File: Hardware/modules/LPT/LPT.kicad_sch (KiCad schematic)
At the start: 17 parts, among them J1 DB25_Receptacle, J2 Bus_PCI_6502, U1 74HC138, U2 74HC138, U3 74HC00, U4 74AHC541, U5 74HCT574, U6 74HCT574, U7 74HC02

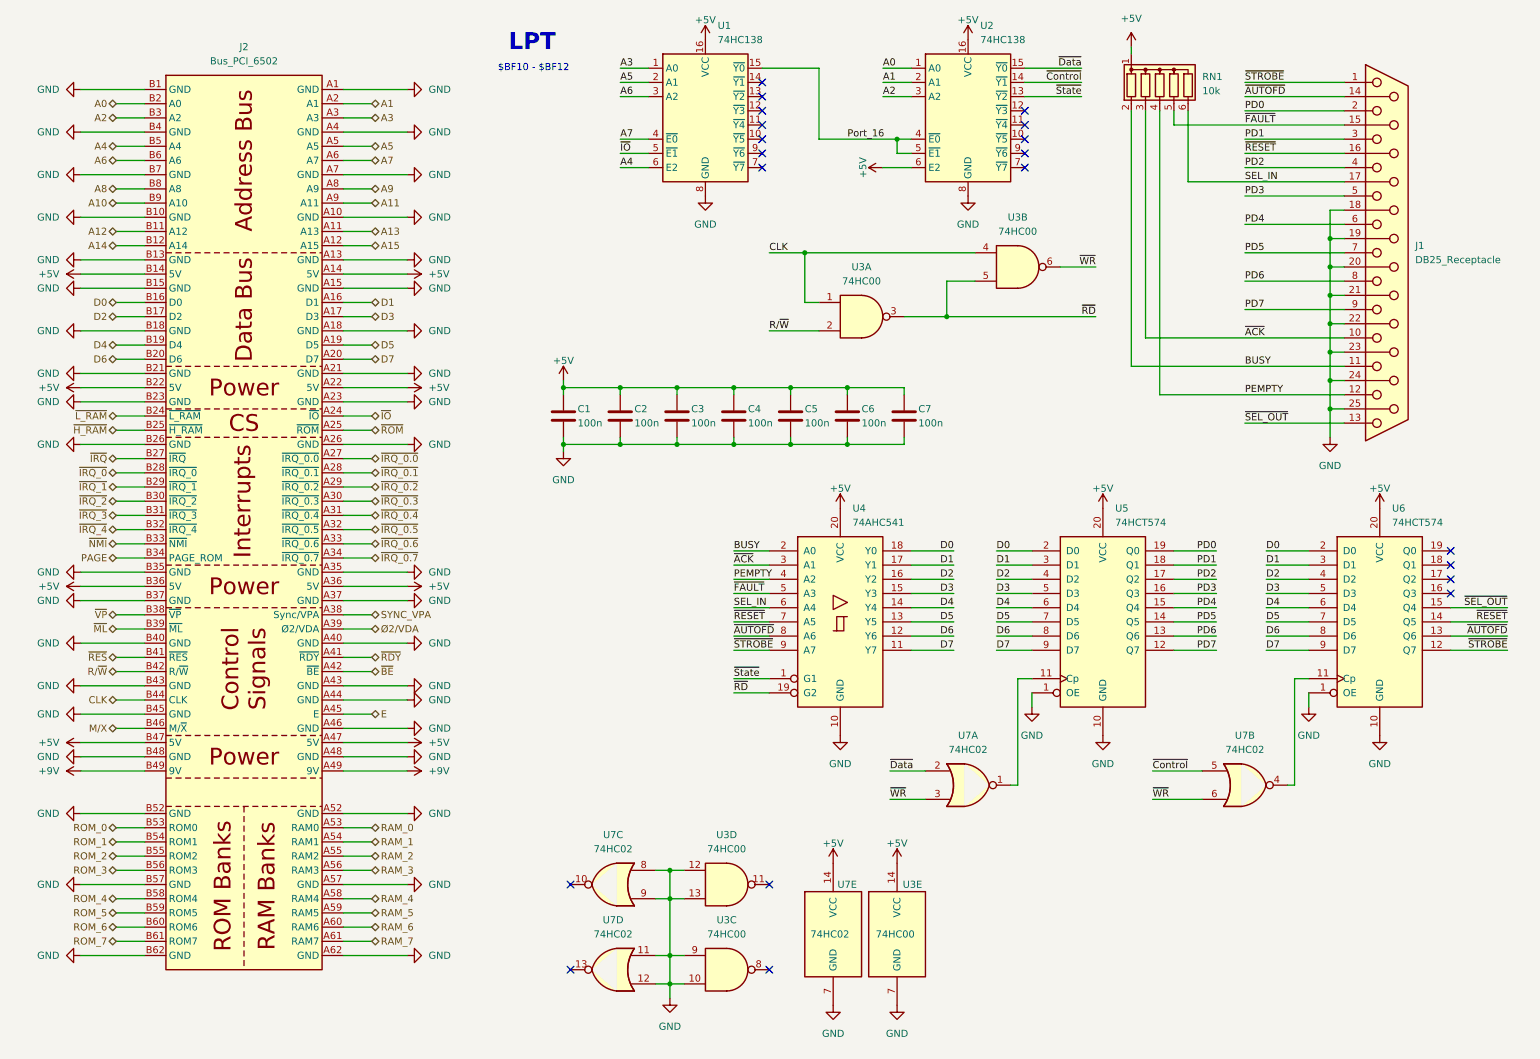
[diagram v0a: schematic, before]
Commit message: Hardware Update Add MyCPU VGA Module Beautify all Schematics minor Error corrections Readme Update
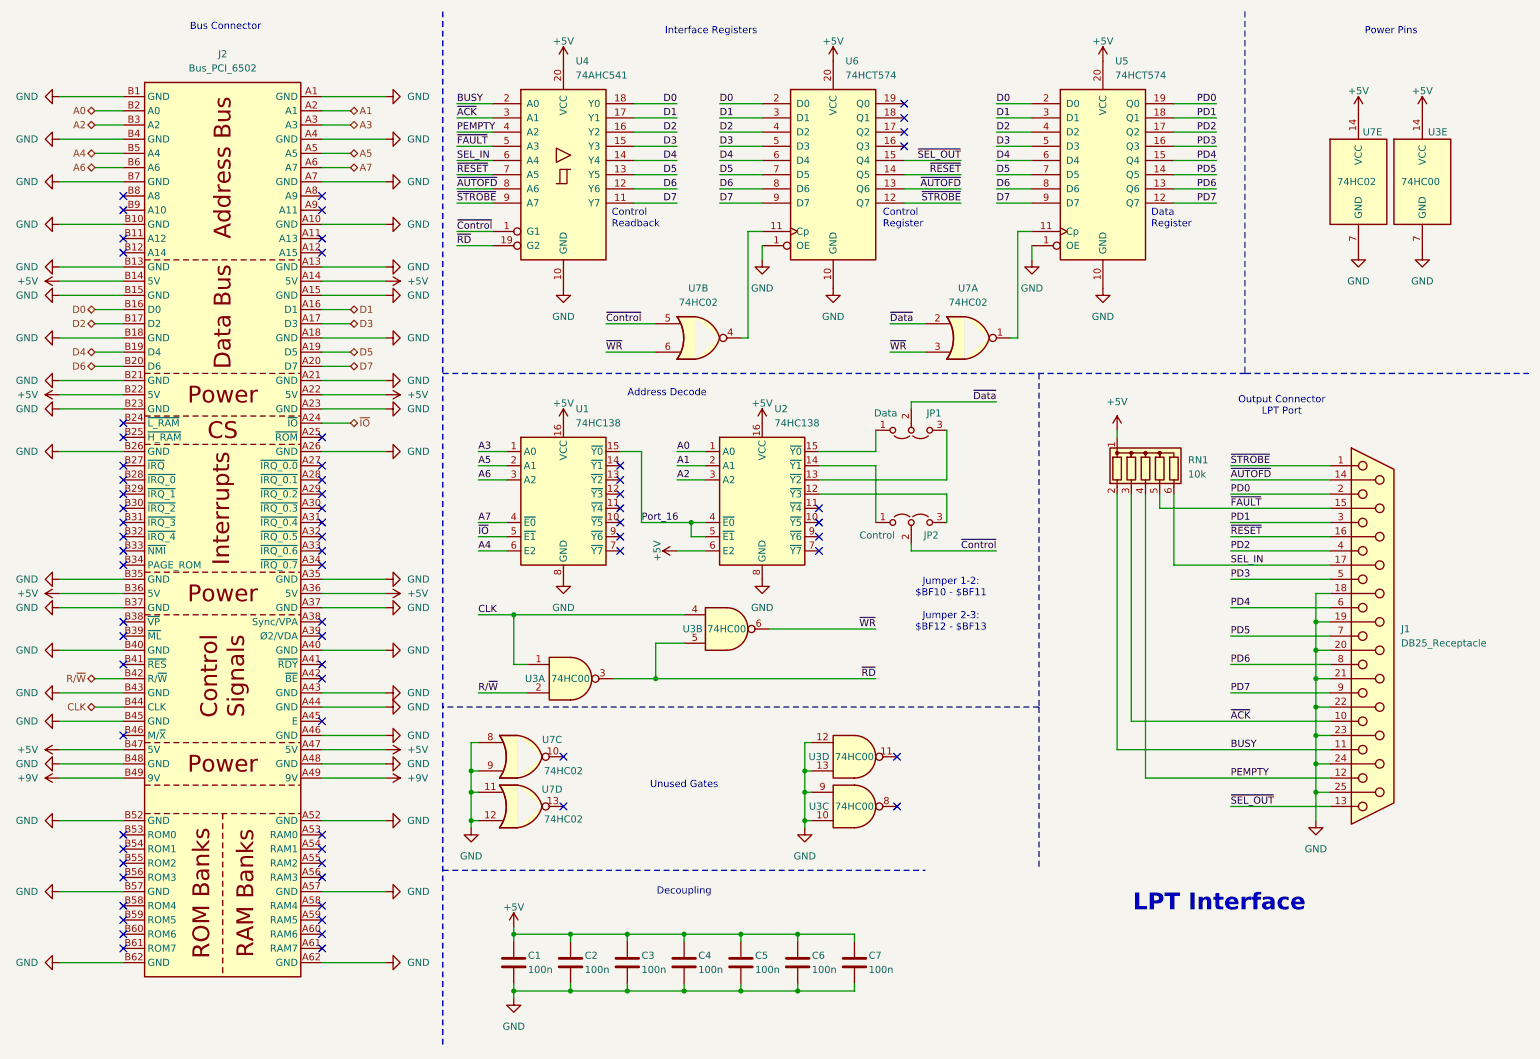
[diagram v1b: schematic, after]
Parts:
- added JP1: Data, Jumper:SolderJumper-3_P2.0mm_Open_TrianglePad1.0x1.5mm_NumberLabels, symbol Jumper:Jumper_3_Open
- added JP2: Control, Jumper:SolderJumper-3_P2.0mm_Open_TrianglePad1.0x1.5mm_NumberLabels, symbol Jumper:Jumper_3_Open
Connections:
- net ~{Control}: now also U4.1 (G1), JP2.2 (C); no longer U2.14 (~{Y1})
- net ~{Data}: now also JP1.2 (C); no longer U2.15 (~{Y0})
- net at U2.12 (~{Y3}): now also JP2.3 (B)
- net A10: no longer names the net of J2.B9 (A10)
- net A11: no longer names the net of J2.A9 (A11)
- net A12: no longer names the net of J2.B11 (A12)
- net A13: no longer names the net of J2.A11 (A13)
- net A14: no longer names the net of J2.B12 (A14)
- net A15: no longer names the net of J2.A12 (A15)
- net A8: no longer names the net of J2.B8 (A8)
- net A9: no longer names the net of J2.A8 (A9)
- net E: no longer names the net of J2.A45 (E)
- net M/X: no longer names the net of J2.B46 (M/~{X})
- net PAGE: no longer names the net of J2.B34 (PAGE_ROM)
- net RAM_0: no longer names the net of J2.A53 (RAM0)
- net RAM_1: no longer names the net of J2.A54 (RAM1)
- net RAM_2: no longer names the net of J2.A55 (RAM2)
- net RAM_3: no longer names the net of J2.A56 (RAM3)
- net RAM_4: no longer names the net of J2.A58 (RAM4)
- net RAM_5: no longer names the net of J2.A59 (RAM5)
- net RAM_6: no longer names the net of J2.A60 (RAM6)
- net RAM_7: no longer names the net of J2.A61 (RAM7)
- net ROM_0: no longer names the net of J2.B53 (ROM0)
- net ROM_1: no longer names the net of J2.B54 (ROM1)
- net ROM_2: no longer names the net of J2.B55 (ROM2)
- net ROM_3: no longer names the net of J2.B56 (ROM3)
- net ROM_4: no longer names the net of J2.B58 (ROM4)
- net ROM_5: no longer names the net of J2.B59 (ROM5)
- net ROM_6: no longer names the net of J2.B60 (ROM6)
- net ROM_7: no longer names the net of J2.B61 (ROM7)
- net SYNC_VPA: no longer names the net of J2.A38 (Sync/VPA)
- net ~{BE}: no longer names the net of J2.A42 (~{BE})
- net ~{H_RAM}: no longer names the net of J2.B25 (~{H_RAM})
- net ~{IRQ_0.0}: no longer names the net of J2.A27 (~{IRQ_0.0})
- net ~{IRQ_0.1}: no longer names the net of J2.A28 (~{IRQ_0.1})
- net ~{IRQ_0.2}: no longer names the net of J2.A29 (~{IRQ_0.2})
- net ~{IRQ_0.3}: no longer names the net of J2.A30 (~{IRQ_0.3})
- net ~{IRQ_0.4}: no longer names the net of J2.A31 (~{IRQ_0.4})
- net ~{IRQ_0.5}: no longer names the net of J2.A32 (~{IRQ_0.5})
- net ~{IRQ_0.6}: no longer names the net of J2.A33 (~{IRQ_0.6})
- net ~{IRQ_0.7}: no longer names the net of J2.A34 (~{IRQ_0.7})
- net ~{IRQ_0}: no longer names the net of J2.B28 (~{IRQ_0})
- net ~{IRQ_1}: no longer names the net of J2.B29 (~{IRQ_1})
- net ~{IRQ_2}: no longer names the net of J2.B30 (~{IRQ_2})
- net ~{IRQ_3}: no longer names the net of J2.B31 (~{IRQ_3})
- net ~{IRQ_4}: no longer names the net of J2.B32 (~{IRQ_4})
- net ~{IRQ}: no longer names the net of J2.B27 (~{IRQ})
- net ~{L_RAM}: no longer names the net of J2.B24 (~{L_RAM})
- net ~{ML}: no longer names the net of J2.B39 (~{ML})
- net ~{NMI}: no longer names the net of J2.B33 (~{NMI})
- net ~{RDY}: no longer names the net of J2.A41 (~{RDY})
- net ~{RES}: no longer names the net of J2.B41 (~{RES})
- net ~{ROM}: no longer names the net of J2.A25 (~{ROM})
- net ~{State}: no longer names the net of U2.13 (~{Y2})
- net ~{State}: now also JP1.3 (B); no longer U4.1 (G1)
- net ~{VP}: no longer names the net of J2.B38 (~{VP})
- net Ø2/VDA: no longer names the net of J2.A39 (Ø2/VDA)
- new net: JP2.1 (A), U2.14 (~{Y1})
- new net: JP1.1 (A), U2.15 (~{Y0})
- no-connect marks 20 -> 71
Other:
- note added: "Address Decode"
- note added: "Bus Connector"
- note added: "Control Readback"
- note added: "Control Register"
- note added: "Data Register"
- note added: "Decoupling"
- note added: "Interface Registers"
- note added: "Jumper 1-2: $BF10 - $BF11 Jumper 2-3: $BF12 - $BF13"
- note added: "LPT Interface"
- note added: "Output Connector LPT Port"
- note added: "Power Pins"
- note added: "Unused Gates"
- note removed: "$BF10 - $BF12"
- note removed: "LPT"
- company: (none) -> Synthron
- title: (none) -> S65xx Computer System
- moved on the sheet: C1, C2, C3, C4, C5, C6, C7, J1, J2, RN1, U1, U2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

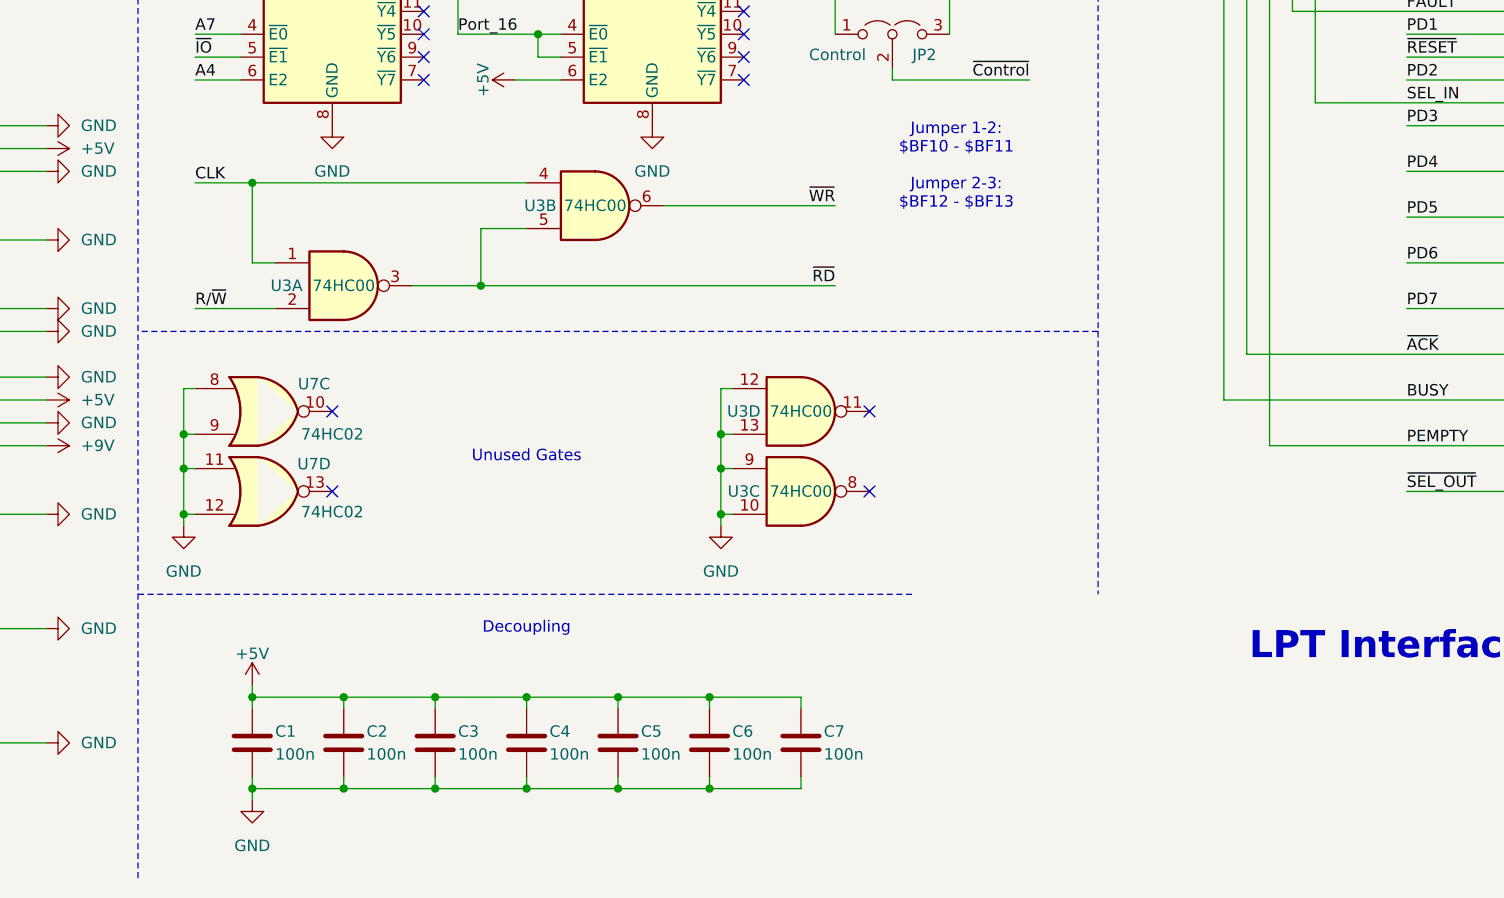
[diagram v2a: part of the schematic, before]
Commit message: Hardware Review Pt. 1 fix Address Decoding for Strobe Generators add bulk capacitance to every board fix wiring of Prototyping Board
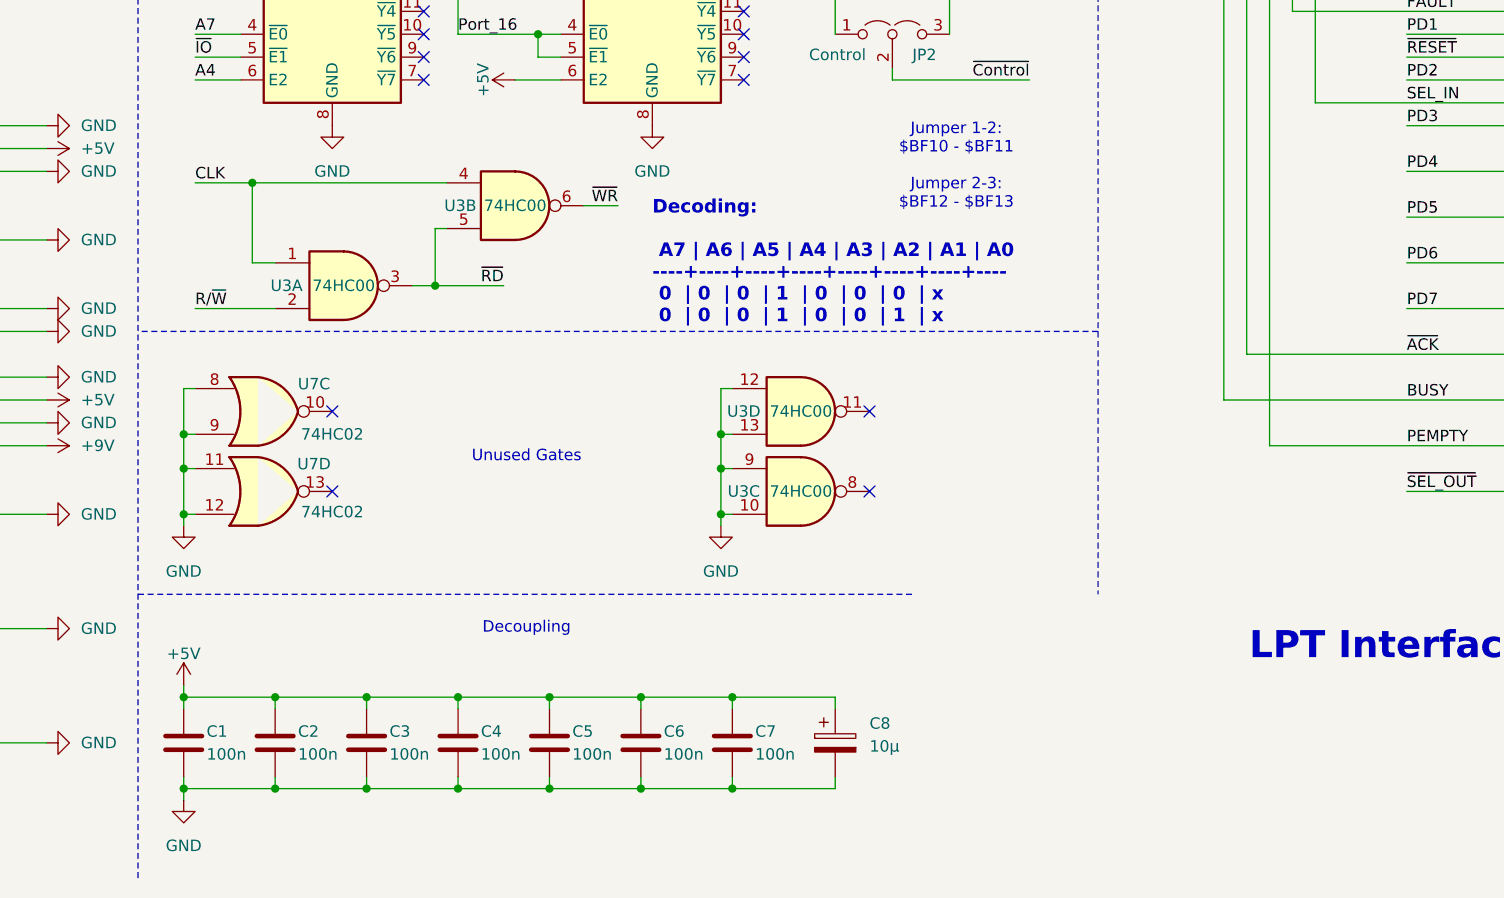
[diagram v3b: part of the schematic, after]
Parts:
- added C8: 10µ, Capacitor_THT:CP_Radial_D5.0mm_P2.50mm, symbol Device:C_Polarized
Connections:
- net +5V: now also C8.1
- net GND: now also C8.2
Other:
- note added: "Decoding: A7 | A6 | A5 | A4 | A3 | A2 | A1 | A0 ----+----+----+----+----+----+----+---- 0 | 0 | 0 | 1 | 0 | 0 | 0 | x 0 | 0 | 0 | 1 | 0 | 0 | 1 | x"
- moved on the sheet: C1, C2, C3, C4, C5, C6, C7, U3B
